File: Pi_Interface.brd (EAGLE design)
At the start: 65 x 56.5 mm, 35 parts, among them IC1 A0 / GP, IC2 A1 / GS, J3 RASPI-40HAT, Q3 BSS138W-7-F, Q4 BSS138W-7-F, Q5 BSS138W-7-F, SW1 SPST_TACT-PT645, SW2 SPST_TACT-PT645

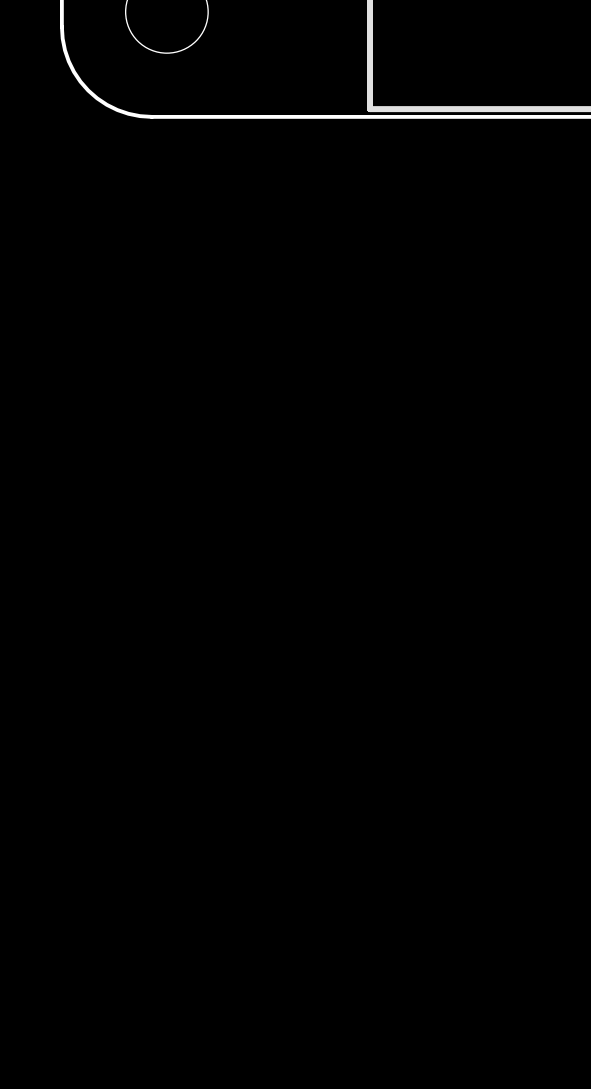
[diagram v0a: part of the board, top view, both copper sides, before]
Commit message: Wired up opto-isolators
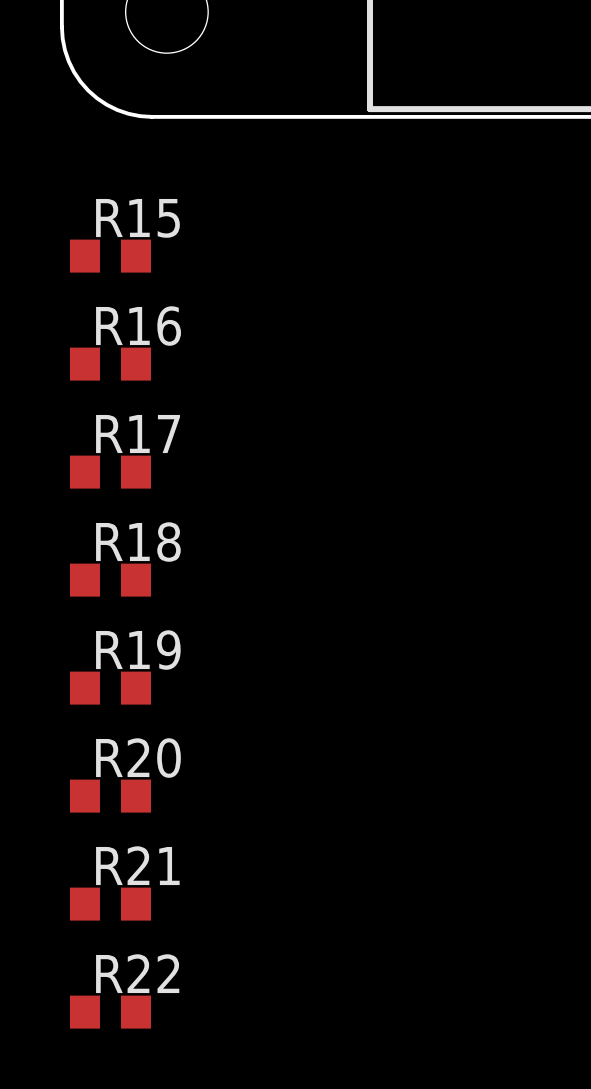
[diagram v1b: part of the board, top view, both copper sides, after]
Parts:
- added R15, R16, R17, R18, R19, R20, R21, R22: (no value), rcl:R0603
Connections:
- new net +3V3: J3.1, J3.17
- new net GNDIO: J-IN.5, OP1.2, OP1.4, OP1.6, OP1.8
- new net N$10: J-OUT.2, OP2.13
- new net N$11: J-OUT.3, OP2.11
- new net N$12: J-OUT.4, OP2.9
- new net N$13: OP2.1, R15.2
- new net N$14: OP2.3, R16.2
- new net N$15: OP2.5, R17.2
- new net N$16: OP2.7, R18.2
- new net N$17: OP1.1, R19.1
- new net N$18: OP1.3, R20.1
- new net N$19: OP1.5, R21.1
- new net N$20: OP1.7, R22.1
- new net N$21: J-IN.1, R19.2
- new net N$22: J-IN.2, R20.2
- new net N$23: J-IN.3, R21.2
- new net N$24: J-IN.4, R22.2
- new net N$9: J-OUT.1, OP2.15
- new net SCL: IC1.5, IC2.5, J3.5
- new net SDA: IC1.4, IC2.4, J3.3
- net +24V: now also OP2.10, OP2.12, OP2.14, OP2.16
- net GND: now also OP2.2, OP2.4, OP2.6, OP2.8; no longer J-IN.5

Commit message: Added 1206 resistor networks to minimize component count on board
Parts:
- removed R1, R10, R2, R3, R4, R8, R9: 100R, rcl:R0603
- removed R15, R16, R17, R18: (no value), rcl:R0603
- added R31, R32: 10k, rcl:R0603
- added R33, R34: 330R, rcl:R0603
- added RN1, RN2, RN5: 330R, resistor-network:RESCAV80P315X160X60-8N
- added RN3: 330R, resistor-network:RESCAXS80P315X160X60-8N
- added RN4: 10K, resistor-network:RESCAXS80P315X160X60-8N
- D1, D2: value 5.1V -> 3V6; device diode:SMB -> zener-diodes:SOD3716X115N
- R11, R13: value 100R -> 10k
- R12, R14: value 100R -> 4k99
- R5, R6, R7: device rcl:R0805 -> rcl:R0603
- moved R22 77.6 mm to (51.4, 30.6)
- moved R21 72.2 mm to (51.4, 27.0)
- moved R20 66.9 mm to (51.4, 23.2)
- moved R19 62.3 mm to (51.4, 19.6)
- moved OP2 34.6 mm to (13.6, 17.2), turned to 270 degrees
- moved OP1 32.0 mm to (44.2, 31.0), turned to 180 degrees
- moved R11 26.9 mm to (50.4, 40.0)
- moved R13 20.6 mm to (50.4, 45.2)
- moved R12 18.0 mm to (41.6, 40.6), turned to 270 degrees
- moved R14 12.3 mm to (41.6, 45.6), turned to 270 degrees
- moved IC1 9.78 mm to (35.6, 40.8), turned to 180 degrees
- moved IC2 9.67 mm to (35.4, 45.4), turned to 180 degrees
- moved J-SRV1 7.00 mm to (29.8, 19.0)
- moved J-SRV2 7.00 mm to (33.6, 19.0)
- moved J-SRV4 7.00 mm to (41.4, 19.0)
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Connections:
- new net IN1: J3.29, RN3.4
- new net IN2: J3.31, RN3.3
- new net IN3: J3.26, RN3.2
- new net IN4: J3.24, RN3.1
- new net N$25: OP1.16, RN3.5, RN4.5
- new net N$26: R32.1, R34.2, SW2.B
- new net N$27: OP1.14, RN3.6, RN4.6
- new net N$29: OP1.12, RN3.7, RN4.7
- new net N$31: OP1.10, RN3.8, RN4.8
- new net N$32: R31.1, R33.2, SW1.B
- new net OUT1: J3.36, RN2.4
- new net OUT2: J3.11, RN2.3
- new net OUT3: J3.12, RN2.2
- new net OUT4: J3.35, RN2.1
- new net SERVO1: J3.38, RN1.4
- new net SERVO2: J3.40, RN1.3
- new net SERVO3: J3.15, RN1.2
- new net SERVO4: J3.16, RN1.1
- new net SWITCH1: J3.32, R33.1
- new net SWITCH2: J3.33, R34.1
- net +3V3: now also IC1.1, IC2.1, R31.2, R32.2, RN4.1, RN4.2, RN4.3, RN4.4
- net +5V: no longer IC1.1, IC2.1
- net GND: now also D1.2, D2.2, OP1.11, OP1.13, OP1.15, OP1.9, SW1.A, SW2.A; no longer D1.A, D2.A
- net N$1: now also RN1.5; no longer R1.2
- net N$10: now also OP2.11; no longer OP2.13
- net N$11: now also OP2.13; no longer OP2.11
- net N$12: now also OP2.15; no longer OP2.9
- net N$13: now also OP2.7, RN2.5; no longer OP2.1, R15.2
- net N$14: now also OP2.5, RN2.6; no longer OP2.3, R16.2
- net N$15: now also OP2.3, RN2.7; no longer OP2.5, R17.2
- net N$16: now also OP2.1, RN2.8; no longer OP2.7, R18.2
- net N$2: now also RN1.6; no longer R2.2
- net N$3: now also RN1.7; no longer R3.2
- net N$4: now also RN1.8; no longer R4.2
- net N$5: now also D1.1; no longer D1.C
- net N$6: now also D2.1; no longer D2.C
- net N$9: now also OP2.9; no longer OP2.15
- net RGB-B: now also J3.23, RN5.1; no longer R10.1
- net RGB-B-GATE: now also RN5.8; no longer R10.2
- net RGB-G: now also J3.19, RN5.3; no longer R9.1
- net RGB-G-GATE: now also RN5.6; no longer R9.2
- net RGB-R: now also J3.21, RN5.2; no longer R8.1
- net RGB-R-GATE: now also RN5.7; no longer R8.2

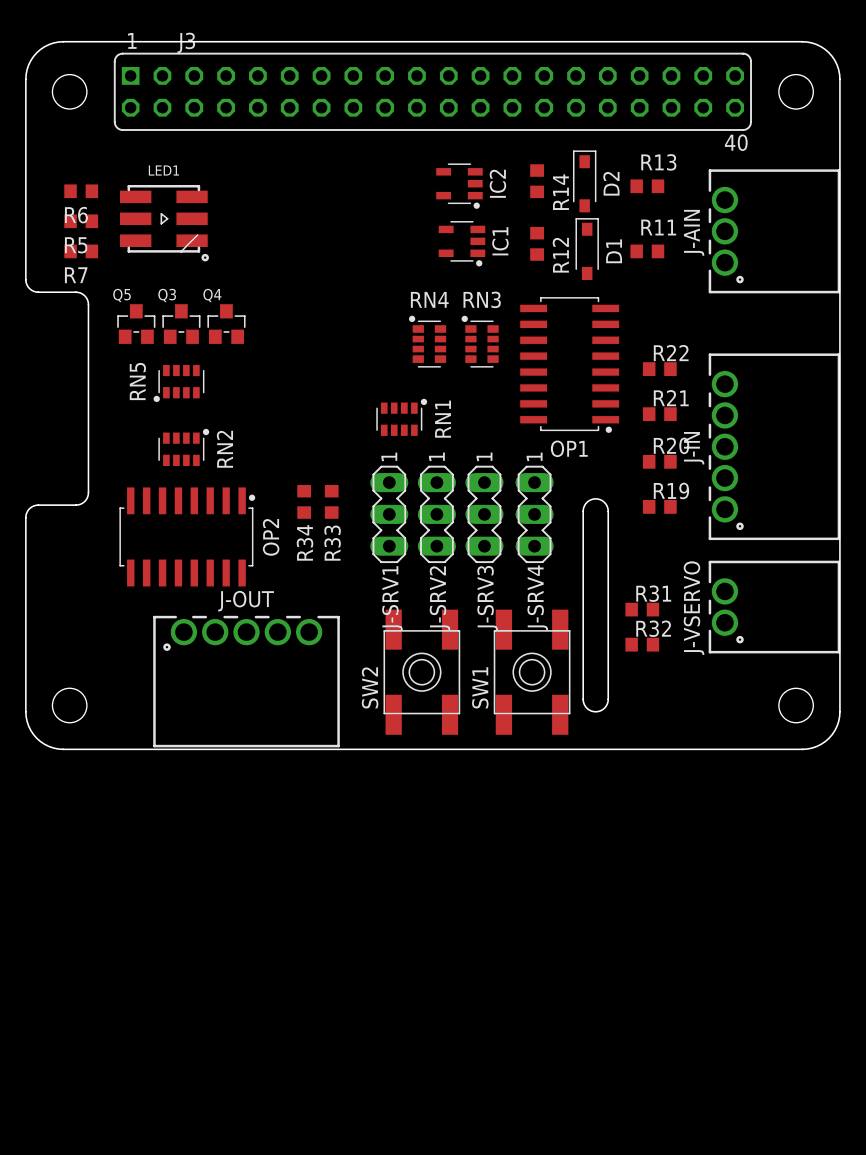
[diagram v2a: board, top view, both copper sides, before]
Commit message: Changed Layout, added EEPROM
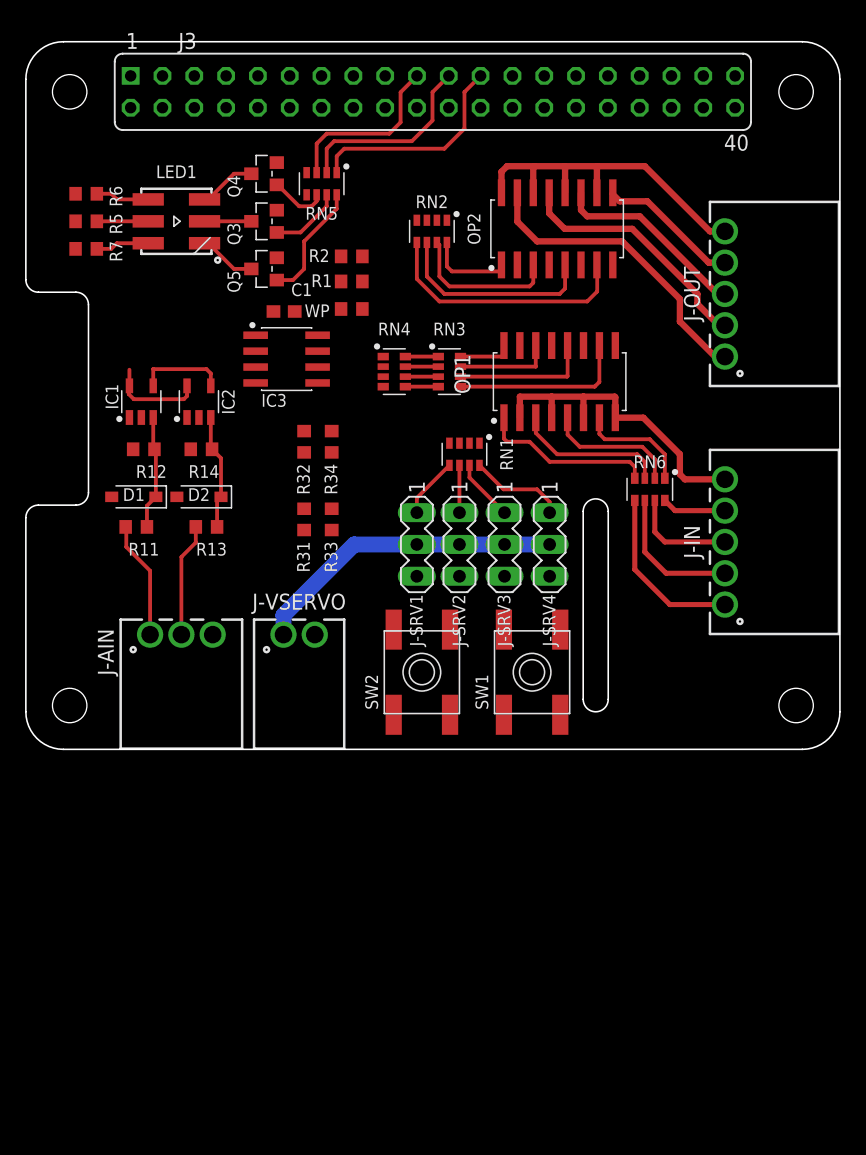
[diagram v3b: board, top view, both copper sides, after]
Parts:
- removed R19, R20, R21, R22: (no value), rcl:R0603
- added C1: 100n, rcl:C0603
- added IC3: 24C32I-GW, eeprom:SOIC127P600X175-8N
- added R1, R2: 3k9, rcl:R0603
- added RN6: 560R, resistor-network:RESCAXS80P315X160X60-8N
- added WP: 0R, rcl:R0603
- moved J-AIN 54.0 mm to (13.2, 9.40), turned to 0 degrees
- moved J-OUT 46.8 mm to (56.6, 36.6), turned to 90 degrees
- moved R11 46.4 mm to (9.60, 18.0), turned to 180 degrees
- moved R13 44.5 mm to (15.2, 18.0), turned to 180 degrees
- moved D1 41.2 mm to (9.40, 20.4), turned to 180 degrees
- moved D2 39.7 mm to (14.6, 20.4), turned to 180 degrees
- moved OP2 38.5 mm to (43.2, 41.8), turned to 90 degrees
- moved R12 35.4 mm to (10.2, 24.2), turned to 180 degrees
- moved R14 34.3 mm to (14.8, 24.2), turned to 180 degrees
- moved J-VSERVO 34.1 mm to (22.6, 9.40), turned to 0 degrees
- moved R32 31.5 mm to (23.0, 24.8), turned to 90 degrees
- moved IC1 28.6 mm to (10.0, 28.0), turned to 90 degrees
- moved R31 27.9 mm to (23.0, 18.6), turned to 90 degrees
- moved IC2 27.1 mm to (14.6, 28.0), turned to 90 degrees
- moved RN2 26.5 mm to (33.2, 41.6)
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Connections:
- net N$7 renamed AIN1
- net N$8 renamed AIN2
- new net ID_SCL: IC3.6, J3.28, R1.1
- new net ID_SDA: IC3.5, J3.27, R2.1
- new net WP: IC3.7, WP.1
- net +3V3: now also C1.1, IC3.8, R1.2, R2.2, WP.2
- net GND: now also C1.2, IC3.1, IC3.2, IC3.3, IC3.4
- net IN1: now also J3.7, RN3.1, RN4.8; no longer J3.29, RN3.4
- net IN2: now also J3.29, RN3.2, RN4.7; no longer J3.31, RN3.3
- net IN3: now also RN3.3, RN4.6; no longer RN3.2
- net IN4: now also RN3.4, RN4.5; no longer RN3.1
- net N$10: now also OP2.13; no longer OP2.11
- net N$11: now also OP2.11; no longer OP2.13
- net N$12: now also OP2.9; no longer OP2.15
- net N$17: now also RN6.4; no longer R19.1
- net N$18: now also RN6.3; no longer R20.1
- net N$19: now also RN6.2; no longer R21.1
- net N$20: now also RN6.1; no longer R22.1
- net N$21: now also RN6.5; no longer R19.2
- net N$22: now also RN6.6; no longer R20.2
- net N$23: now also RN6.7; no longer R21.2
- net N$24: now also RN6.8; no longer R22.2
- net N$25: now also OP1.10; no longer OP1.16, RN4.5
- net N$27: now also OP1.12; no longer OP1.14, RN4.6
- net N$29: now also OP1.14; no longer OP1.12, RN4.7
- net N$31: now also OP1.16; no longer OP1.10, RN4.8
- net N$9: now also OP2.15; no longer OP2.9
- net OUT1: now also J3.12, RN2.1; no longer J3.36, RN2.4
- net OUT2: now also J3.35, RN2.2; no longer J3.11, RN2.3
- net OUT3: now also J3.38, RN2.3; no longer J3.12, RN2.2
- net OUT4: now also J3.40, RN2.4; no longer J3.35, RN2.1
- net SERVO1: now also J3.15; no longer J3.38
- net SERVO2: now also J3.16; no longer J3.40
- net SERVO3: now also J3.18; no longer J3.15
- net SERVO4: now also J3.22; no longer J3.16
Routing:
- net +24V: track 0.00 -> 28.3 mm
- net GNDIO: track 0.00 -> 26.0 mm
- net V+: track 0.00 -> 25.1 mm
- net N$9: track 0.00 -> 24.4 mm
- net N$16: track 0.00 -> 20.5 mm
- net N$10: track 0.00 -> 19.8 mm
- net RGB-B: track 0.00 -> 17.2 mm
- net N$15: track 0.00 -> 16.4 mm
- net N$11: track 0.00 -> 15.7 mm
- net RGB-R: track 0.00 -> 15.4 mm
- net N$25: track 0.00 -> 14.2 mm
- net RGB-G: track 0.00 -> 14.0 mm
- net N$17: track 0.00 -> 14.0 mm
- net N$21: track 0.00 -> 13.9 mm
- net N$18: track 0.00 -> 12.2 mm
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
